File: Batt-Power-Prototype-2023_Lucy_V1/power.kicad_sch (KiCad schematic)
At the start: 61 parts, among them J1 Conn_01x02_Pin, U1 RPA60-2412SFW, U3 AZ1117IH-5.0, U5 AP62250Z6, U5 AZ1117-3.3

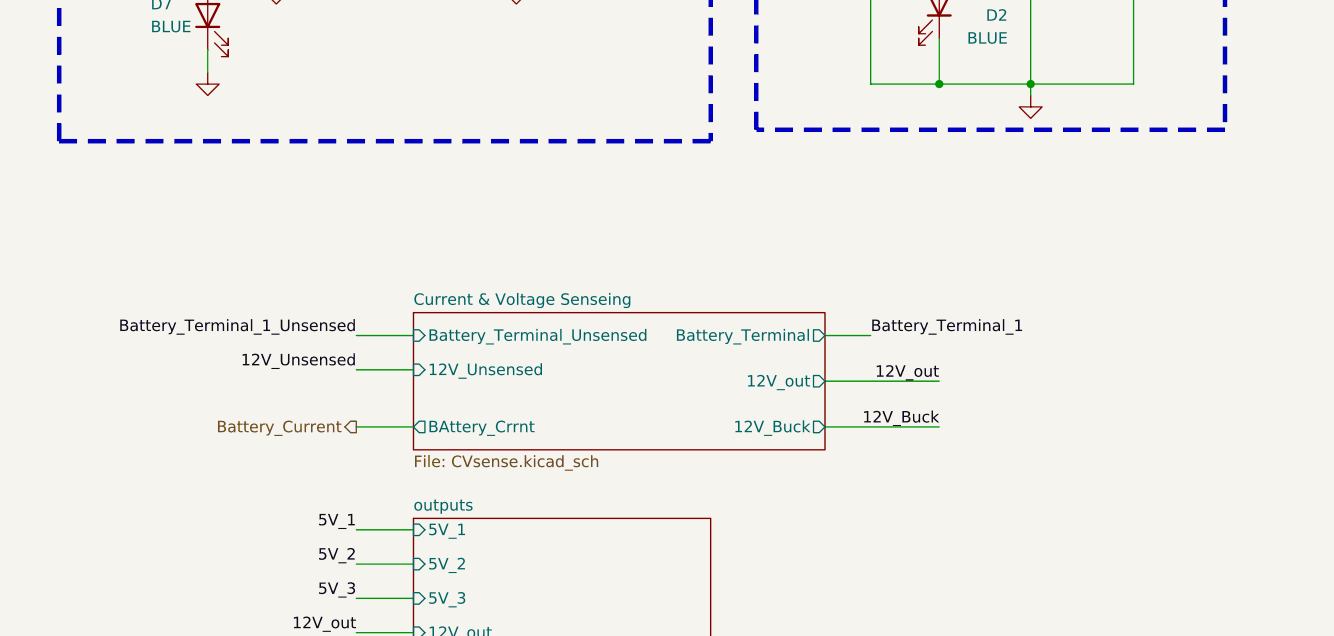
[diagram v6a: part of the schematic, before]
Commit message: no more global variables
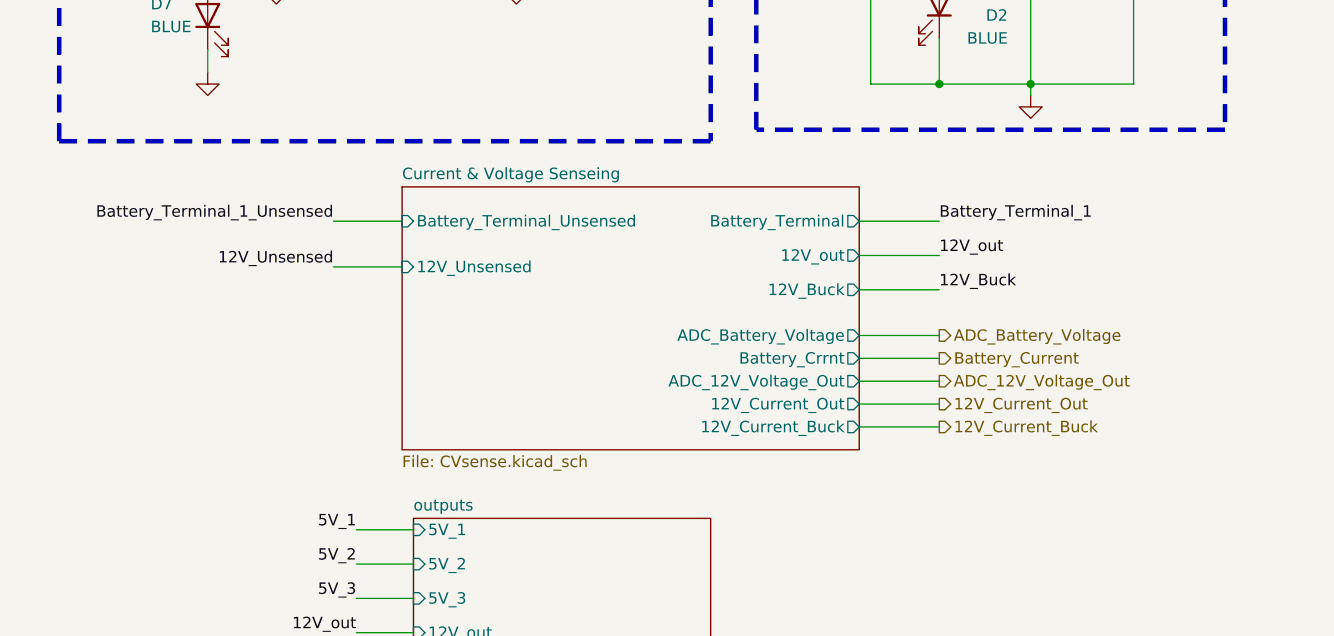
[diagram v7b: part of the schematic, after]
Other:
- sheet Current & Voltage Senseing ports: added 12V_Current_Buck, 12V_Current_Out, ADC_12V_Voltage_Out, ADC_Battery_Voltage, Battery_Crrnt; removed BAttery_Crrnt
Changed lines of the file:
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@@
     (stroke (width 0) (type default))
   )
-  (wire (pts (xy 100.33 152.4) (xy 105.41 152.4))
+  (wire (pts (xy 104.14 139.7) (xy 113.03 139.7))
     (stroke (width 0) (type default))
   )
@@
     (stroke (width 0) (type default))
   )
-  (wire (pts (xy 113.03 157.48) (xy 100.33 157.48))
+  (wire (pts (xy 113.03 143.51) (xy 104.14 143.51))
     (stroke (width 0) (type default))
   )
@@
     (stroke (width 0) (type default))
   )
+  (wire (pts (xy 45.72 139.7) (xy 53.34 139.7))
+    (stroke (width 0) (type default))
+  )
   (wire (pts (xy 180.34 76.2) (xy 185.42 76.2))
     (stroke (width 0) (type default))
@@
     (stroke (width 0) (type default))
   )
-  (wire (pts (xy 48.26 156.21) (xy 54.61 156.21))
+  (wire (pts (xy 45.72 144.78) (xy 53.34 144.78))
     (stroke (width 0) (type default))
   )
@@
     (stroke (width 0) (type default))
   )
+  (wire (pts (xy 104.14 160.02) (xy 113.03 160.02))
+    (stroke (width 0) (type default))
+  )
   (wire (pts (xy 142.24 54.61) (xy 147.32 54.61))
     (stroke (width 0) (type default))
@@
     (stroke (width 0) (type default))
   )
+  (wire (pts (xy 104.14 157.48) (xy 113.03 157.48))
+    (stroke (width 0) (type default))
+  )
   (wire (pts (xy 134.62 93.98) (xy 134.62 102.87))
     (stroke (width 0) (type default))
@@
     (stroke (width 0) (type default))
   )
+  (wire (pts (xy 104.14 152.4) (xy 113.03 152.4))
+    (stroke (width 0) (type default))
+  )
   (wire (pts (xy 102.87 54.61) (xy 102.87 55.88))
     (stroke (width 0) (type default))
@@
     (stroke (width 0) (type default))
   )
-  (wire (pts (xy 265.43 90.17) (xy 265.43 106.68))
+  (wire (pts (xy 104.14 162.56) (xy 113.03 162.56))
     (stroke (width 0) (type default))
   )
-  (wire (pts (xy 100.33 162.56) (xy 113.03 162.56))
+  (wire (pts (xy 265.43 90.17) (xy 265.43 106.68))
     (stroke (width 0) (type default))
   )
-  (wire (pts (xy 190.5 30.48) (xy 194.31 30.48))
+  (wire (pts (xy 104.14 147.32) (xy 113.03 147.32))
     (stroke (width 0) (type default))
   )
-  (wire (pts (xy 48.26 152.4) (xy 54.61 152.4))
+  (wire (pts (xy 190.5 30.48) (xy 194.31 30.48))
     (stroke (width 0) (type default))
   )
@@
     (stroke (width 0) (type default))
   )
+  (wire (pts (xy 104.14 154.94) (xy 113.03 154.94))
+    (stroke (width 0) (type default))
+  )
   (wire (pts (xy 214.63 81.28) (xy 214.63 95.25))
     (stroke (width 0) (type default))
@@
     (stroke (width 0) (type default))
   )
-  (wire (pts (xy 48.26 162.56) (xy 54.61 162.56))
-    (stroke (width 0) (type default))
-  )
   (wire (pts (xy 74.93 35.56) (xy 83.82 35.56))
     (stroke (width 0) (type default))
@@
     (effects (font (size 1.27 1.27)) (justify left bottom))
   )
-  (label "Battery_Terminal_1_Unsensed" (at 48.26 152.4 180) (fields_autoplaced)
+  (label "Battery_Terminal_1_Unsensed" (at 45.72 139.7 180) (fields_autoplaced)
     (effects (font (size 1.27 1.27)) (justify right bottom))
   )
@@
     (effects (font (size 1.27 1.27)) (justify left bottom))
   )
-  (label "12V_out" (at 113.03 157.48 180) (fields_autoplaced)
-    (effects (font (size 1.27 1.27)) (justify right bottom))
+  (label "12V_out" (at 113.03 143.51 0) (fields_autoplaced)
+    (effects (font (size 1.27 1.27)) (justify left bottom))
   )
   (label "5V_3" (at 48.26 181.61 180) (fields_autoplaced)
@@
     (effects (font (size 1.27 1.27)) (justify left bottom))
   )
-  (label "12V_Buck" (at 113.03 162.56 180) (fields_autoplaced)
-    (effects (font (size 1.27 1.27)) (justify right bottom))
+  (label "12V_Buck" (at 113.03 147.32 0) (fields_autoplaced)
+    (effects (font (size 1.27 1.27)) (justify left bottom))
   )
   (label "5V_2" (at 275.59 72.39 0) (fields_autoplaced)
     (effects (font (size 1.27 1.27)) (justify left bottom))
   )
-  (label "Battery_Terminal_1" (at 105.41 152.4 0) (fields_autoplaced)
+  (label "Battery_Terminal_1" (at 113.03 139.7 0) (fields_autoplaced)
     (effects (font (size 1.27 1.27)) (justify left bottom))
   )
-  (label "12V_Unsensed" (at 48.26 156.21 180) (fields_autoplaced)
+  (label "12V_Unsensed" (at 45.72 144.78 180) (fields_autoplaced)
     (effects (font (size 1.27 1.27)) (justify right bottom))
   )
@@
     (effects (font (size 1.27 1.27)) (justify right bottom))
   )
-  (hierarchical_label "Battery_Current" (shape output) (at 48.26 162.56 180) (fields_autoplaced)
-    (effects (font (size 1.27 1.27)) (justify right))
+  (hierarchical_label "ADC_12V_Voltage_Out" (shape output) (at 113.03 157.48 0) (fields_autoplaced)
+    (effects (font (size 1.27 1.27)) (justify left))
+  )
+  (hierarchical_label "12V_Current_Buck" (shape output) (at 113.03 162.56 0) (fields_autoplaced)
+    (effects (font (size 1.27 1.27)) (justify left))
+  )
+  (hierarchical_label "Battery_Current" (shape output) (at 113.03 154.94 0) (fields_autoplaced)
+    (effects (font (size 1.27 1.27)) (justify left))
+  )
+  (hierarchical_label "ADC_Battery_Voltage" (shape output) (at 113.03 152.4 0) (fields_autoplaced)
+    (effects (font (size 1.27 1.27)) (justify left))
+  )
+  (hierarchical_label "12V_Current_Out" (shape output) (at 113.03 160.02 0) (fields_autoplaced)
+    (effects (font (size 1.27 1.27)) (justify left))
   )
   (symbol (lib_id "Device:C_Polarized") (at 264.16 40.64 0) (unit 1)
@@
       (effects (font (size 1.27 1.27)) hide)
     )
-    (pin "2")
     (pin "1")
+    (pin "2")
     (pin "3")
     (instances
@@
     )
   )
-  (sheet (at 54.61 149.86) (size 45.72 15.24) (fields_autoplaced)
+  (sheet (at 53.34 135.89) (size 50.8 29.21) (fields_autoplaced)
     (stroke (width 0.1524) (type solid))
     (fill (color 0 0 0 0.0000))
-    (property "Sheetname" "Current & Voltage Senseing" (at 54.61 149.1484 0)
+    (property "Sheetname" "Current & Voltage Senseing" (at 53.34 135.1784 0)
       (effects (font (size 1.27 1.27)) (justify left bottom))
     )
-    (property "Sheetfile" "CVsense.kicad_sch" (at 54.61 165.6846 0)
+    (property "Sheetfile" "CVsense.kicad_sch" (at 53.34 165.6846 0)
       (effects (font (size 1.27 1.27)) (justify left top))
     )
-    (pin "12V_Buck" output (at 100.33 162.56 0)
+    (pin "12V_Buck" output (at 104.14 147.32 0)
       (effects (font (size 1.27 1.27)) (justify right))
     )
-    (pin "12V_Unsensed" input (at 54.61 156.21 180)
+    (pin "12V_Unsensed" input (at 53.34 144.78 180)
       (effects (font (size 1.27 1.27)) (justify left))
     )
-    (pin "12V_out" output (at 100.33 157.48 0)
+    (pin "12V_out" output (at 104.14 143.51 0)
       (effects (font (size 1.27 1.27)) (justify right))
     )
-    (pin "Battery_Terminal_Unsensed" input (at 54.61 152.4 180)
+    (pin "Battery_Terminal_Unsensed" input (at 53.34 139.7 180)
       (effects (font (size 1.27 1.27)) (justify left))
     )
-    (pin "Battery_Terminal" output (at 100.33 152.4 0)
+    (pin "Battery_Terminal" output (at 104.14 139.7 0)
       (effects (font (size 1.27 1.27)) (justify right))
     )
-    (pin "BAttery_Crrnt" output (at 54.61 162.56 180)
-      (effects (font (size 1.27 1.27)) (justify left))
+    (pin "Battery_Crrnt" output (at 104.14 154.94 0)
+      (effects (font (size 1.27 1.27)) (justify right))
+    )
+    (pin "12V_Current_Out" output (at 104.14 160.02 0)
+      (effects (font (size 1.27 1.27)) (justify right))
+    )
+    (pin "ADC_12V_Voltage_Out" output (at 104.14 157.48 0)
+      (effects (font (size 1.27 1.27)) (justify right))
+    )
+    (pin "12V_Current_Buck" output (at 104.14 162.56 0)
+      (effects (font (size 1.27 1.27)) (justify right))
+    )
+    (pin "ADC_Battery_Voltage" output (at 104.14 152.4 0)
+      (effects (font (size 1.27 1.27)) (justify right))
     )
     (instances

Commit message: some of the touch ups
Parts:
- removed C?, ECA-1VM102B3: 1m, Capacitor_THT:CP_Radial_D12.5mm_P5.00mm, symbol Device:C_Polarized
- removed U5 (x2): AP62250Z6, Package_TO_SOT_SMD:SOT-563, symbol Regulator_Switching:AP62250Z6
- added C20, C34: 1m, Capacitor_THT:CP_Radial_D12.5mm_P5.00mm, symbol Device:C_Polarized
- added F2, F3, F4, F5: 3544-2, BP_FTP:CONN_3544-2_KEY, symbol Device:Fuse
- added U? (x2): AP62250Z6, Package_TO_SOT_SMD:SOT-563, symbol Regulator_Switching:AP62250Z6
- C48: renamed from ECA-1VM102B2; Digikey # (none) -> P10387TB-ND
- C49: renamed from CESH107M100AH4AA1; digikey # (none) -> 399-ESH107M100AH4AA-ND
- C50: renamed from ECA-1VM102B1; Digikey # (none) -> P10387TB-ND
- U?: renamed from U5; Digikey # (none) -> 31-AP62250Z6-7TR-ND
- renumbered C31 to C46, needstobe2kv1 to C47, C18 to C?, C16 to C?, C17 to C?, C15 to C?, C12 to C?, C11 to C?, C21 to C?, C22 to C?, D22 to D10, D21 to D9, D2 to D?, D7 to D?, J1 to J5, L1 to L?, R3 to R10, R4 to R11, R1 to R13, R2 to R14, R19 to R15, R9 to R?, R8 to R?, R10 to R?, R12 to R?, U1 to U7, U3 to U?, U5 to U?
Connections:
- net 12V_Buck: now also U?.1 (VIN), U?.1 (VIN), U?.5 (EN), U?.5 (EN)
- net 5V_1: now also F2.1
- net 5V_2: now also C34.1, F3.1
- net 5V_3: now also C20.1, F4.1
- net GND: now also C20.2, C34.2, U?.3 (GND), U?.3 (GND)
- net at C?.1, L?.1: now also U?.2 (SW) (x2)
- net at C?.2: now also U?.4 (BST) (x2)
- net at R?.2, R?.2: now also U?.6 (FB) (x2)
- new net 12V_PCBs: F5.1
- new net outputs/12V_PCBs: F5.2
- new net outputs/5V_1: F2.2
- new net outputs/5V_2: F3.2
- new net outputs/5V_3: F4.2
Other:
- sheet Current & Voltage Senseing ports: added 12V_PCBs; removed 12V_out
- sheet outputs ports: added 12V_PCBs; removed 12V_out
